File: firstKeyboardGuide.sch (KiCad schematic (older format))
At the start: 5 parts

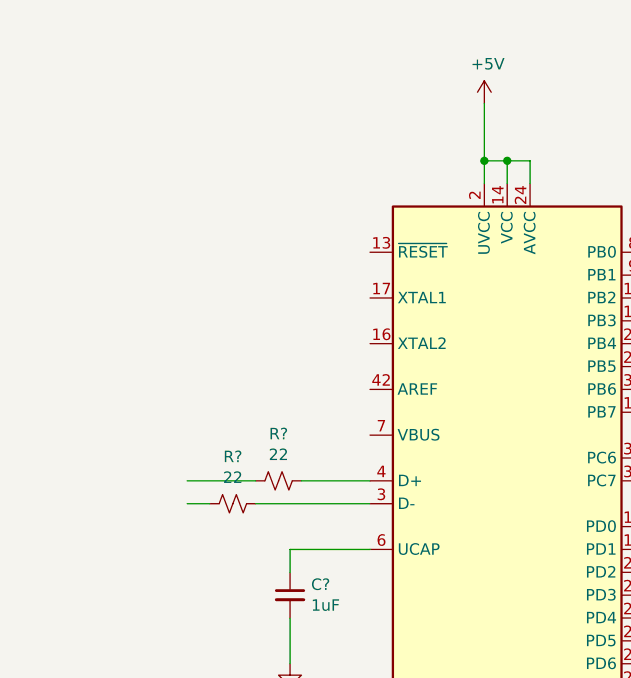
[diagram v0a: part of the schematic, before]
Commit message: Power lines, decoupling capacitors, and mcu crystal
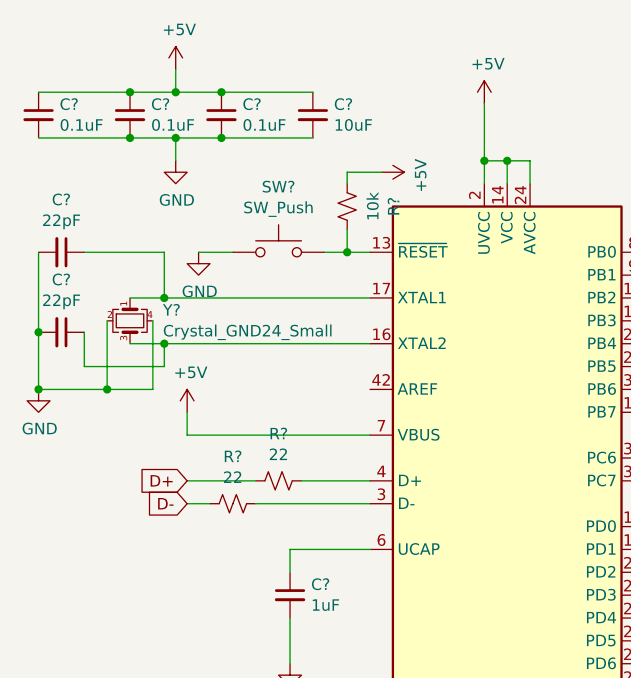
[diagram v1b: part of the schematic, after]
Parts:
- added C? (x3): 0.1uF, symbol Device:C_Small
- added C?: 10uF, symbol Device:C_Small
- added C? (x2): 22pF, symbol Device:C_Small
- added R?: 10k, symbol Device:R_Small_US
- added SW?: SW_Push, symbol Switch:SW_Push
- added Y?: Crystal_GND24_Small, symbol Device:Crystal_GND24_Small
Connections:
- net labels added: D+, D-
- wire segments 20 -> 53
